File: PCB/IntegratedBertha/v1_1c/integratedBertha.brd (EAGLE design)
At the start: 108.1 x 84.6 mm, 100 parts, among them CON1 SPI, IC1 REG1117, IC2 AD8223, J7 22--02, Q1 BSP75, Q2 BSP75, Q4 BSP75, Q5 BSP75, Q6 BSP75, Q7 IRF3704S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

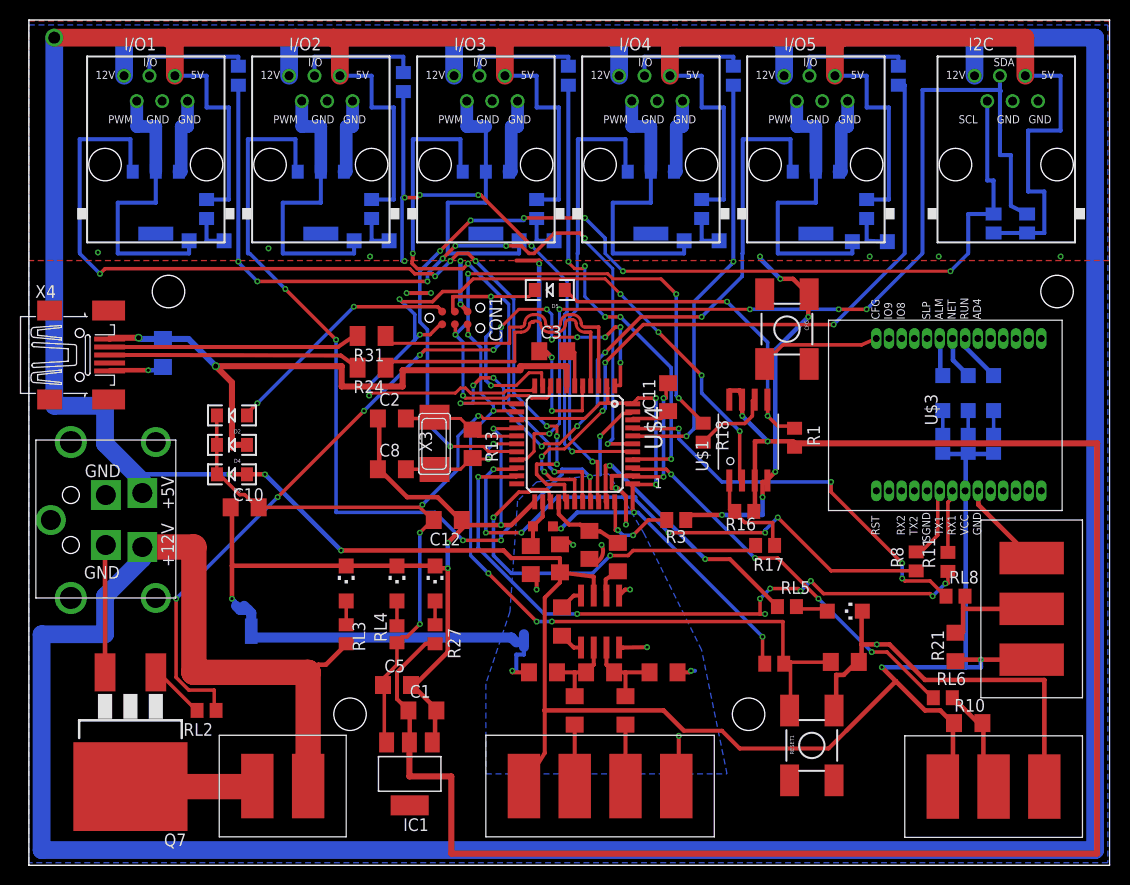
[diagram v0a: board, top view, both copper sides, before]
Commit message: corrected boards to fulfill design rules of the factory in Bogota (drill size and copper spacing. small changes in solardecathlon (SPI pins and design rules changed for zigbee header pads
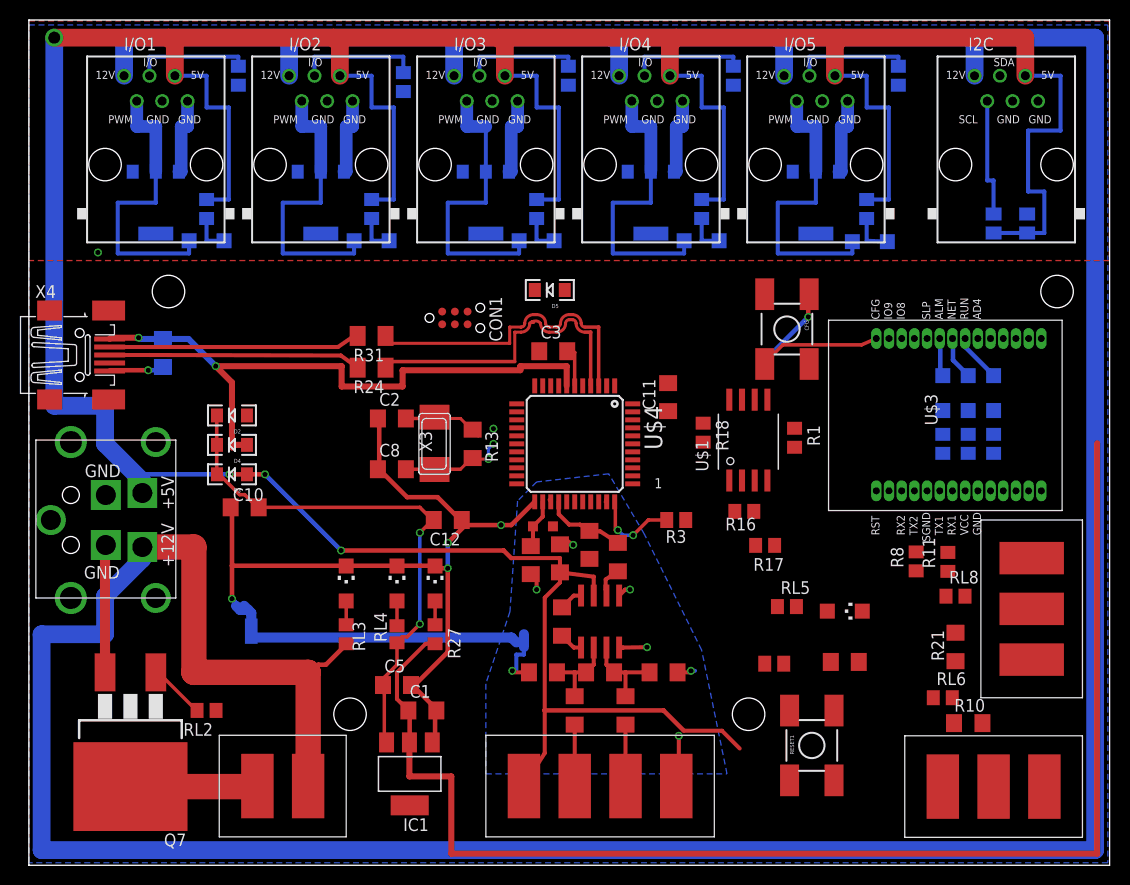
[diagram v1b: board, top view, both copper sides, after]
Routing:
- net GND: track 280.4 -> 152.0 mm, vias 26 -> 8
- net SDA: track 97.2 -> 0.00 mm, vias 5 -> 0
- net D6*: track 94.6 -> 0.00 mm, vias 7 -> 0
- net SCL: track 105.1 -> 11.9 mm, vias 7 -> 0
- net D10*: track 82.3 -> 0.00 mm, vias 5 -> 0
- net D7*: track 81.5 -> 0.00 mm, vias 12 -> 0
- net A3: track 81.0 -> 0.00 mm, vias 8 -> 0
- net +5V: track 479.6 -> 398.9 mm, vias 6 -> 4
- net MISO: track 80.5 -> 0.00 mm, vias 7 -> 0
- net +5V/1: track 130.1 -> 54.3 mm, vias 9 -> 2
- net RESET: track 75.5 -> 0.00 mm, vias 5 -> 0
- net D8*: track 72.1 -> 0.00 mm, vias 5 -> 0
- net D11*: track 71.7 -> 0.00 mm, vias 7 -> 0
- net TX: track 66.1 -> 0.00 mm, vias 9 -> 0
- net A2: track 61.2 -> 0.00 mm, vias 6 -> 0
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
